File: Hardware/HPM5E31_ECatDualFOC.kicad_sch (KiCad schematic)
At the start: 4 parts, among them U34 M3, U38 M3, U46 M3, U47 M3

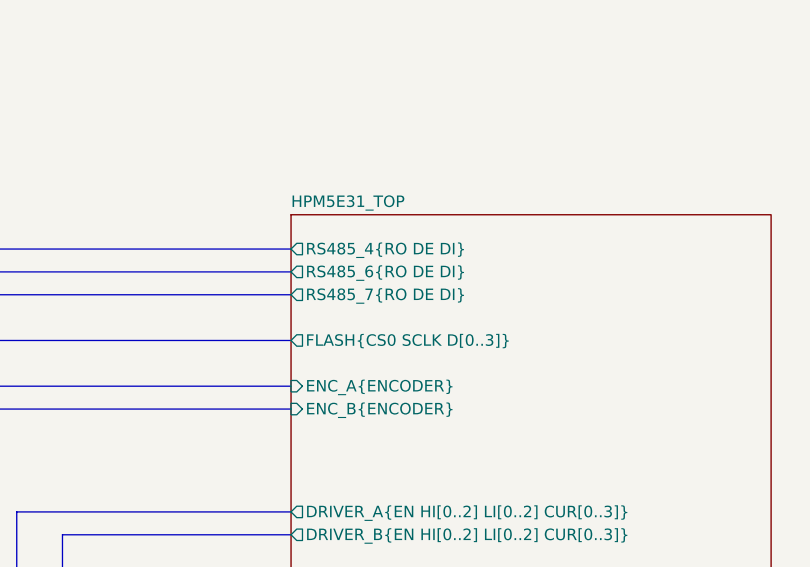
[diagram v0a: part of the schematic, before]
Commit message: 新增ESC IO引出，ESC CTR LED，EUI接口
编码器接口电源输出加保险，SPI加ESD
PY32ADC外部接口加ESD
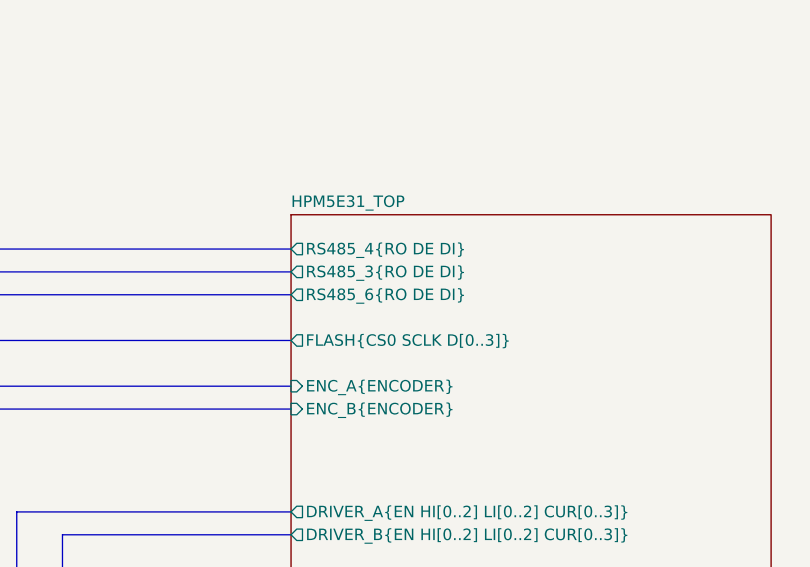
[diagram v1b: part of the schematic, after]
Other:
- sheet HPM5E31_TOP ports: added RS485_3{RO DE DI}; removed RS485_7{RO DE DI}
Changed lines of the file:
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@@
-			)
-		)
-		(pin "RS485_6{RO DE DI}" output
-			(at 129.54 63.5 180)
-			(effects
-				(font
-					(size 1.27 1.27)
-				)
-				(justify left)
-			)
-		)
-		(pin "RS485_7{RO DE DI}" output
-			(at 129.54 66.04 180)
-			(effects
-				(font
-					(size 1.27 1.27)
-				)
-				(justify left)
 			)
 		)
@@
 			(effects
 				(font
+					(size 1.27 1.27)
+				)
+				(justify left)
+			)
+		)
+		(pin "RS485_3{RO DE DI}" output
+			(at 129.54 63.5 180)
+			(effects
+				(font
+					(size 1.27 1.27)
+				)
+				(justify left)
+			)
+		)
+		(pin "RS485_6{RO DE DI}" output
+			(at 129.54 66.04 180)
+			(effects
+				(font

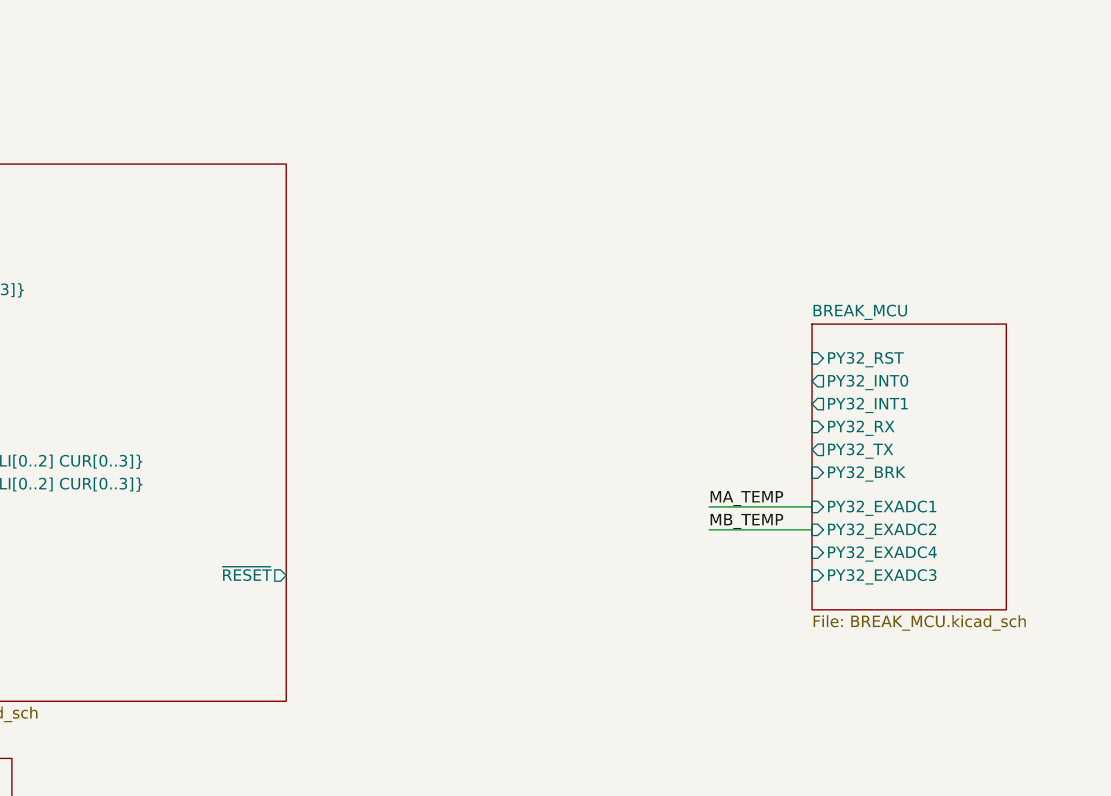
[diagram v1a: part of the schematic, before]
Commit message: 调整引脚，拉线
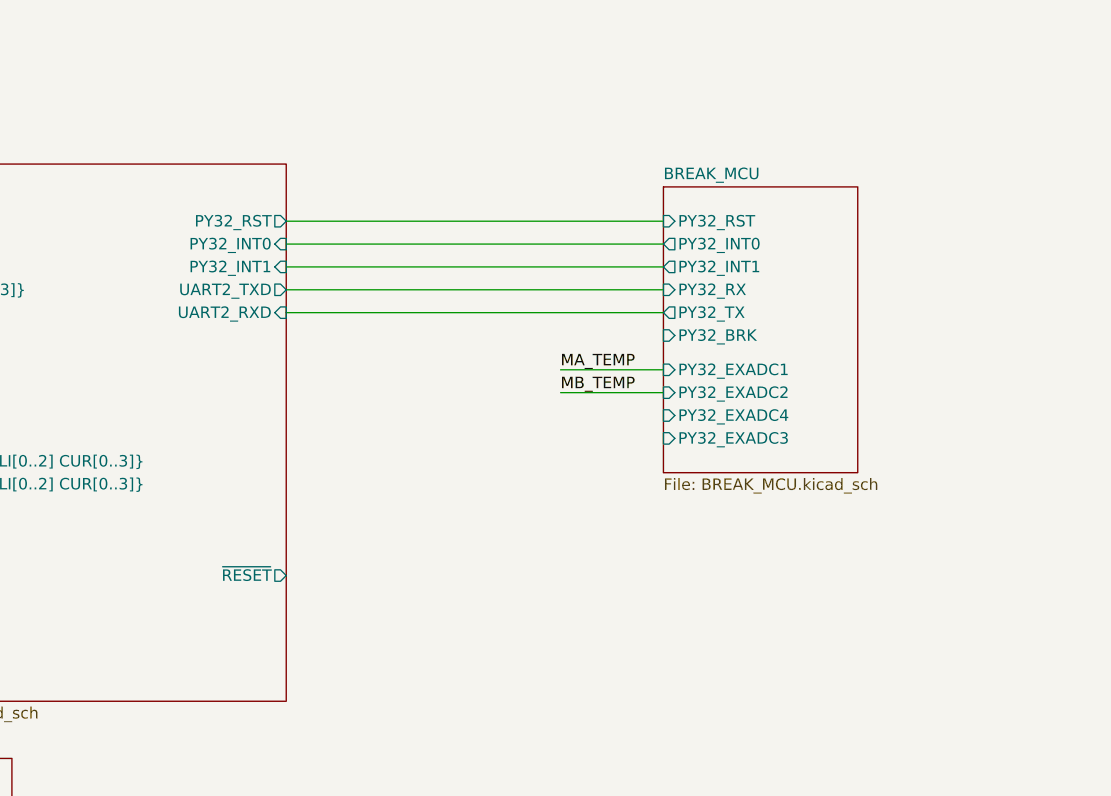
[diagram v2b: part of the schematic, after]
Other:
- sheet HPM5E31_TOP ports: added PY32_INT0, PY32_INT1, PY32_RST, UART2_RXD, UART2_TXD; removed none
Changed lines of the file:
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@@
+		)
+	)
+	(wire
+		(pts
+			(xy 182.88 68.58) (xy 224.79 68.58)
+		)
+		(stroke
+			(width 0)
+			(type default)
 		)
 	)
@@
 		)
 	)
+	(wire
+		(pts
+			(xy 182.88 66.04) (xy 224.79 66.04)
+		)
+		(stroke
+			(width 0)
+			(type default)
+		)
+	)
 	(bus
 		(pts
@@
 		)
 	)
+	(wire
+		(pts
+			(xy 182.88 63.5) (xy 224.79 63.5)
+		)
+		(stroke
+			(width 0)
+			(type default)
+		)
+	)
 	(bus
 		(pts
@@
 	(wire
 		(pts
-			(xy 229.87 97.79) (xy 241.3 97.79)
+			(xy 213.36 82.55) (xy 224.79 82.55)
 		)
 		(stroke
@@
 		)
 	)
+	(wire
+		(pts
+			(xy 182.88 73.66) (xy 224.79 73.66)
+		)
+		(stroke
+			(width 0)
+			(type default)
+		)
+	)
 	(bus
 		(pts
@@
 	(wire
 		(pts
-			(xy 229.87 95.25) (xy 241.3 95.25)
+			(xy 213.36 80.01) (xy 224.79 80.01)
+		)
+		(stroke
+			(width 0)
+			(type default)
+		)
+	)
+	(wire
+		(pts
+			(xy 182.88 71.12) (xy 224.79 71.12)
 		)
 		(stroke
@@
 	)
 	(label "MA_TEMP"
-		(at 229.87 95.25 0)
+		(at 213.36 80.01 0)
 		(effects
 			(font
@@
 	)
 	(label "MB_TEMP"
-		(at 229.87 97.79 0)
+		(at 213.36 82.55 0)
 		(effects
 			(font
@@
 	)
 	(sheet
-		(at 241.3 74.93)
+		(at 224.79 59.69)
 		(size 21.59 31.75)
 		(exclude_from_sim no)
@@
 		)
 		(property "Sheetname" "BREAK_MCU"
-			(at 241.3 74.2184 0)
+			(at 224.79 58.9784 0)
 			(effects
 				(font
@@
 		)
 		(property "Sheetfile" "BREAK_MCU.kicad_sch"
-			(at 241.3 107.2646 0)
+			(at 224.79 92.0246 0)
 			(effects
 				(font
@@
 		)
 		(pin "PY32_INT0" output
-			(at 241.3 81.28 180)
+			(at 224.79 66.04 180)
 			(effects
 				(font
@@
 		)
 		(pin "PY32_INT1" output
-			(at 241.3 83.82 180)
+			(at 224.79 68.58 180)
 			(effects
 				(font
@@
 		)
 		(pin "PY32_RST" input
-			(at 241.3 78.74 180)
+			(at 224.79 63.5 180)
 			(effects
 				(font
@@
 		)
 		(pin "PY32_RX" input
-			(at 241.3 86.36 180)
+			(at 224.79 71.12 180)
 			(effects
 				(font
@@
 		)
 		(pin "PY32_TX" output
-			(at 241.3 88.9 180)
+			(at 224.79 73.66 180)
 			(effects
 				(font
@@
 		)
 		(pin "PY32_EXADC1" input
-			(at 241.3 95.25 180)
+			(at 224.79 80.01 180)
 			(effects
 				(font
@@
 		)
 		(pin "PY32_EXADC3" input
-			(at 241.3 102.87 180)
+			(at 224.79 87.63 180)
 			(effects
 				(font
@@
 		)
 		(pin "PY32_EXADC4" input
-			(at 241.3 100.33 180)
+			(at 224.79 85.09 180)
 			(effects
 				(font
@@
 		)
 		(pin "PY32_EXADC2" input
-			(at 241.3 97.79 180)
+			(at 224.79 82.55 180)
 			(effects
 				(font
@@
 		)
 		(pin "PY32_BRK" input
-			(at 241.3 91.44 180)
+			(at 224.79 76.2 180)
 			(effects
 				(font
@@
 			)
 		)
+		(pin "PY32_INT0" input
+			(at 182.88 66.04 0)
+			(effects
+				(font
+					(size 1.27 1.27)
+				)
+				(justify right)
+			)
+		)
+		(pin "PY32_INT1" input
+			(at 182.88 68.58 0)
+			(effects
+				(font
+					(size 1.27 1.27)
+				)
+				(justify right)
+			)
+		)
+		(pin "PY32_RST" output
+			(at 182.88 63.5 0)
+			(effects
+				(font
+					(size 1.27 1.27)
+				)
+				(justify right)
+			)
+		)
+		(pin "UART2_RXD" input
+			(at 182.88 73.66 0)
+			(effects
+				(font
+					(size 1.27 1.27)
+				)
+				(justify right)
+			)
+		)
+		(pin "UART2_TXD" output
+			(at 182.88 71.12 0)
+			(effects
+				(font
+					(size 1.27 1.27)
+				)
+				(justify right)
+			)
+		)

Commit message: 拉线
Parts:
- added R21: 0R,1%, Resistor_SMD:R_0402_1005Metric, symbol HPM6280Foc:0402WGF0000TCE
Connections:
- new net HPM5E31_TOP/nBREAK: R21.1
- new net nBREAK: R21.2
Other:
- added sheet EMS_BUTTON (EMS_BUTTON.kicad_sch)
- sheet BREAK_MCU ports: added ~{PY32_RST}; removed PY32_RST
- sheet HPM5E31_TOP ports: added nBREAK; removed none
- sheet INVERTER_BRIDGE_A ports: added BREAK; removed none
- sheet INVERTER_BRIDGE_B ports: added BREAK; removed none

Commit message: 修存档拉线
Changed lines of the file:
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@@
 	)
 	(label "MA_TEMP"
-		(at 213.36 80.01 0)
+		(at 213.36 82.55 0)
 		(effects
 			(font
@@
 	)
 	(label "MB_TEMP"
-		(at 213.36 82.55 0)
+		(at 213.36 80.01 0)
 		(effects
 			(font

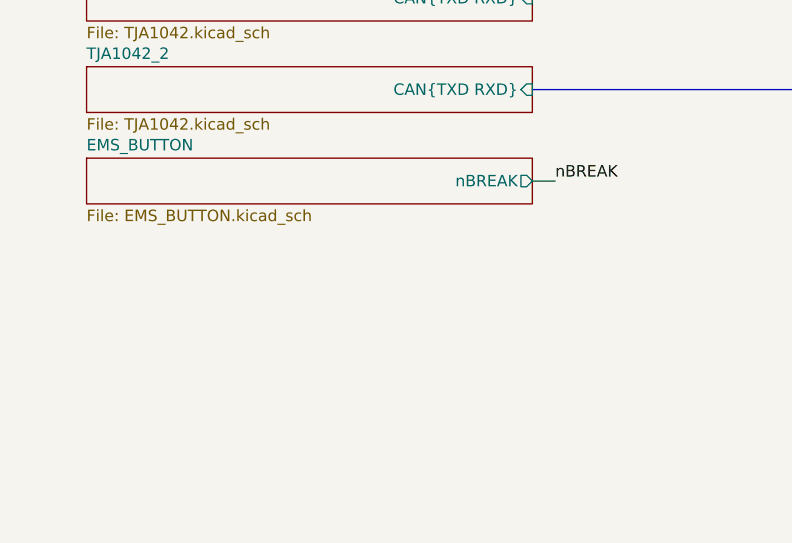
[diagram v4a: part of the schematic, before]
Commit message: 拉线，增加刹车电阻
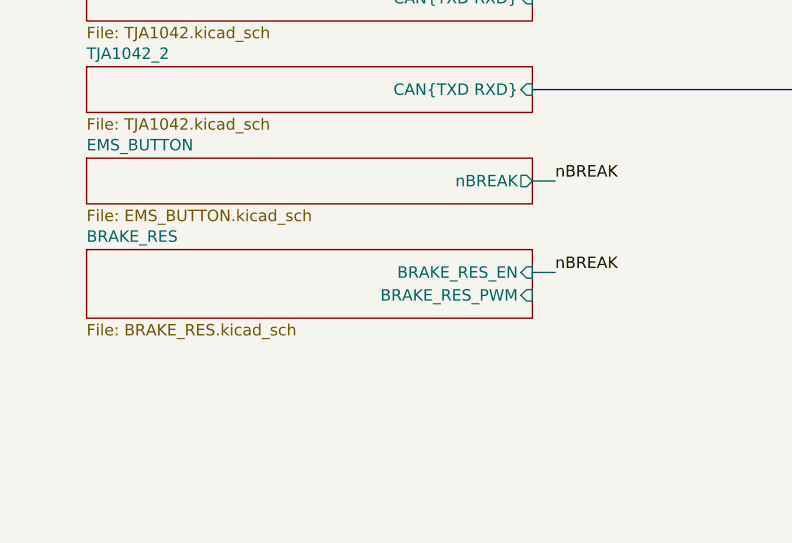
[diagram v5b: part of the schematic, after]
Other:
- added sheet BRAKE_RES (BRAKE_RES.kicad_sch)
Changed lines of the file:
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@@
+		)
+	)
+	(wire
+		(pts
+			(xy 74.93 162.56) (xy 77.47 162.56)
+		)
+		(stroke
+			(width 0)
+			(type default)
 		)
 	)
@@
 		)
 	)
+	(label "nBREAK"
+		(at 77.47 162.56 0)
+		(effects
+			(font
+				(size 1.27 1.27)
+			)
+			(justify left bottom)
+		)
+	)
 	(label "MB_TEMP"
 		(at 213.36 80.01 0)
@@
 				)
 			)
+		)
+	)
+	(sheet
+		(at 25.4 160.02)
+		(size 49.53 7.62)
+		(exclude_from_sim no)
+		(in_bom yes)
+		(on_board yes)
+		(dnp no)
+		(fields_autoplaced yes)
+		(stroke
+			(width 0.1524)
+			(type solid)
+		)
+		(fill
+			(color 0 0 0 0.0000)
+		)
+		(property "Sheetname" "BRAKE_RES"
+			(at 25.4 159.3084 0)
+			(effects
+				(font
+					(size 1.27 1.27)
+				)
+				(justify left bottom)
+			)
+		)
+		(property "Sheetfile" "BRAKE_RES.kicad_sch"
+			(at 25.4 168.2246 0)
+			(effects
+				(font
+					(size 1.27 1.27)
+				)
+				(justify left top)
+			)
+		)
+		(pin "BRAKE_RES_EN" input
+			(at 74.93 162.56 0)
+			(effects
+				(font
+					(size 1.27 1.27)
+				)
+				(justify right)
+			)
+		)
+		(pin "BRAKE_RES_PWM" input
+			(at 74.93 165.1 0)
+			(effects
+				(font
+					(size 1.27 1.27)
+				)
+				(justify right)
+			)
+		)
+		(instances
+			(project "HPM5E31_ECatDualFOC"
+				(path "/a07e9810-3899-4327-ba8f-f24142a7c70e"
+					(page "27")
+				)
+			)

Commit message: 拉线
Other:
- sheet HPM5E31_TOP ports: added BRAKE_RES_PWM; removed none
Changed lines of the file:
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@@
+		)
+	)
+	(wire
+		(pts
+			(xy 118.11 165.1) (xy 74.93 165.1)
+		)
+		(stroke
+			(width 0)
+			(type default)
 		)
 	)
@@
 	(wire
 		(pts
+			(xy 129.54 105.41) (xy 118.11 105.41)
+		)
+		(stroke
+			(width 0)
+			(type default)
+		)
+	)
+	(wire
+		(pts
 			(xy 182.88 63.5) (xy 224.79 63.5)
 		)
@@
 		(pts
 			(xy 152.4 146.05) (xy 154.94 146.05)
+		)
+		(stroke
+			(width 0)
+			(type default)
+		)
+	)
+	(wire
+		(pts
+			(xy 118.11 105.41) (xy 118.11 165.1)
 		)
 		(stroke
@@
 			)
 		)
+		(pin "BRAKE_RES_PWM" output
+			(at 129.54 105.41 180)
+			(effects
+				(font
+					(size 1.27 1.27)
+				)
+				(justify left)
+			)
+		)

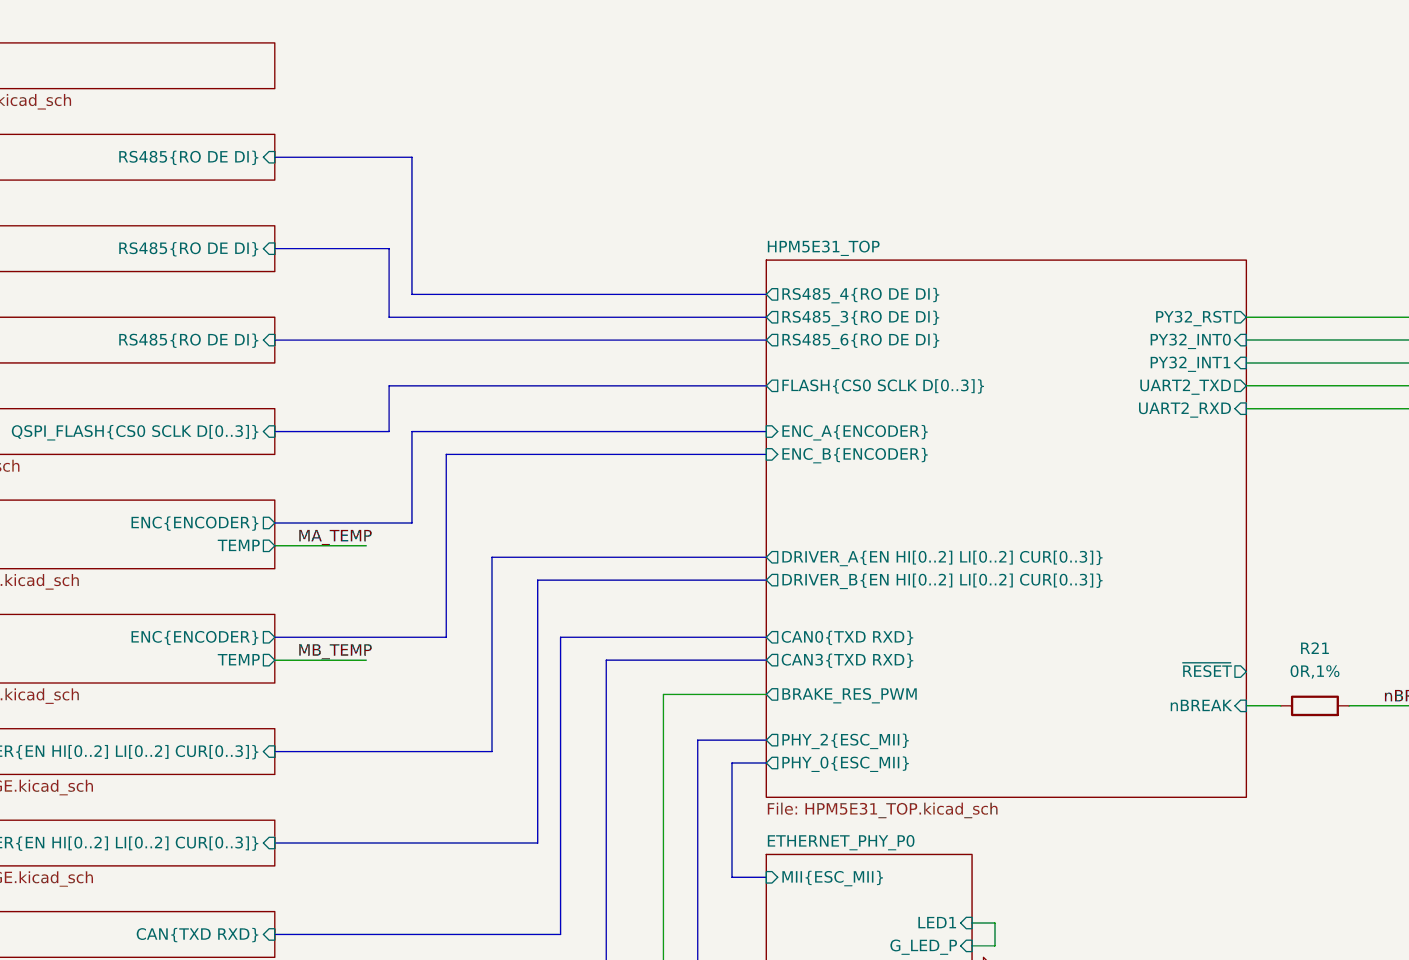
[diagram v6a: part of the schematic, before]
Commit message: 添加母线电压测量
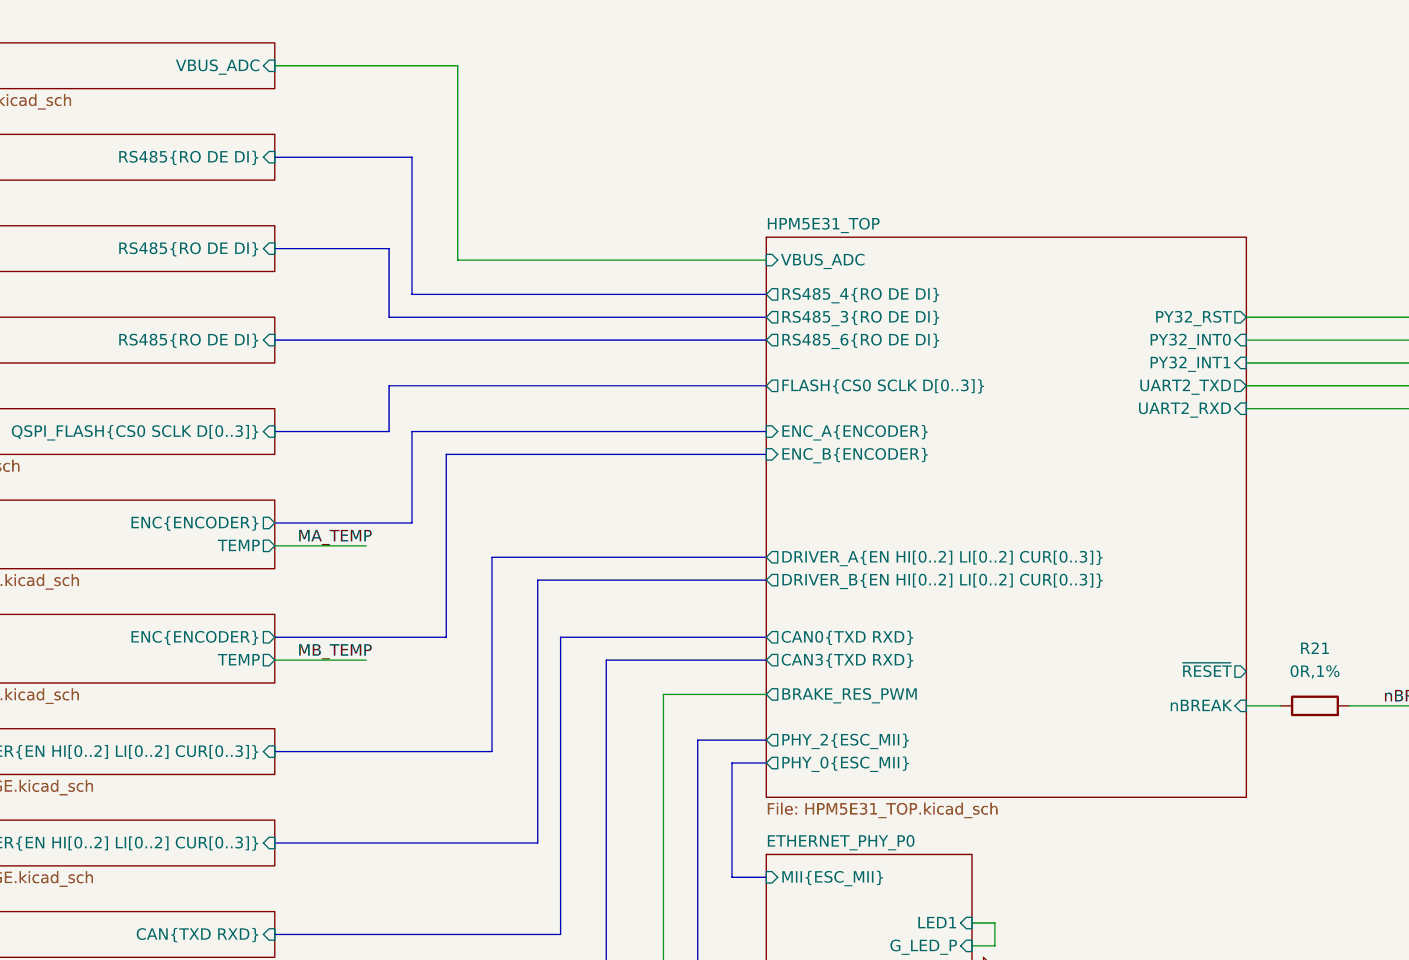
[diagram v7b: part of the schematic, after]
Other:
- sheet HPM5E31_TOP ports: added VBUS_ADC; removed none
- sheet POWER_SUPPLY ports: added VBUS_ADC; removed none
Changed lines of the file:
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@@
 	(wire
 		(pts
+			(xy 74.93 35.56) (xy 95.25 35.56)
+		)
+		(stroke
+			(width 0)
+			(type default)
+		)
+	)
+	(wire
+		(pts
 			(xy 154.94 133.35) (xy 152.4 133.35)
 		)
@@
 	(wire
 		(pts
+			(xy 95.25 35.56) (xy 95.25 57.15)
+		)
+		(stroke
+			(width 0)
+			(type default)
+		)
+	)
+	(wire
+		(pts
 			(xy 152.4 143.51) (xy 154.94 143.51)
 		)
@@
 		(pts
 			(xy 213.36 80.01) (xy 224.79 80.01)
+		)
+		(stroke
+			(width 0)
+			(type default)
+		)
+	)
+	(wire
+		(pts
+			(xy 95.25 57.15) (xy 129.54 57.15)
 		)
 		(stroke
@@
 			)
 		)
+		(pin "VBUS_ADC" input
+			(at 74.93 35.56 0)
+			(effects
+				(font
+					(size 1.27 1.27)
+				)
+				(justify right)
+			)
+		)
 		(instances
 			(project "HPM5E31_ECatDualFOC"
@@
 	)
 	(sheet
-		(at 129.54 57.15)
-		(size 53.34 59.69)
+		(at 129.54 54.61)
+		(size 53.34 62.23)
 		(exclude_from_sim no)
 		(in_bom yes)
@@
 		)
 		(property "Sheetname" "HPM5E31_TOP"
-			(at 129.54 56.4384 0)
+			(at 129.54 53.8984 0)
 			(effects
 				(font
@@
 			(effects
 				(font
+					(size 1.27 1.27)
+				)
+				(justify left)
+			)
+		)
+		(pin "VBUS_ADC" input
+			(at 129.54 57.15 180)
+			(effects
+				(font
